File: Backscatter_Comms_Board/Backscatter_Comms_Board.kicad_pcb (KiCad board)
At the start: 2 copper layers, 38.5 x 33.9 mm, 48 parts, among them J1 SPK_IN, J2 Conn_01x09, J3 Conn_01x02, M1 MNMOS, M2 DNP, T1 SP-48, U1 ADG919BRMZ, U2 ADG841YKSZ-REEL7, U3 NCS2200SQ2T2G

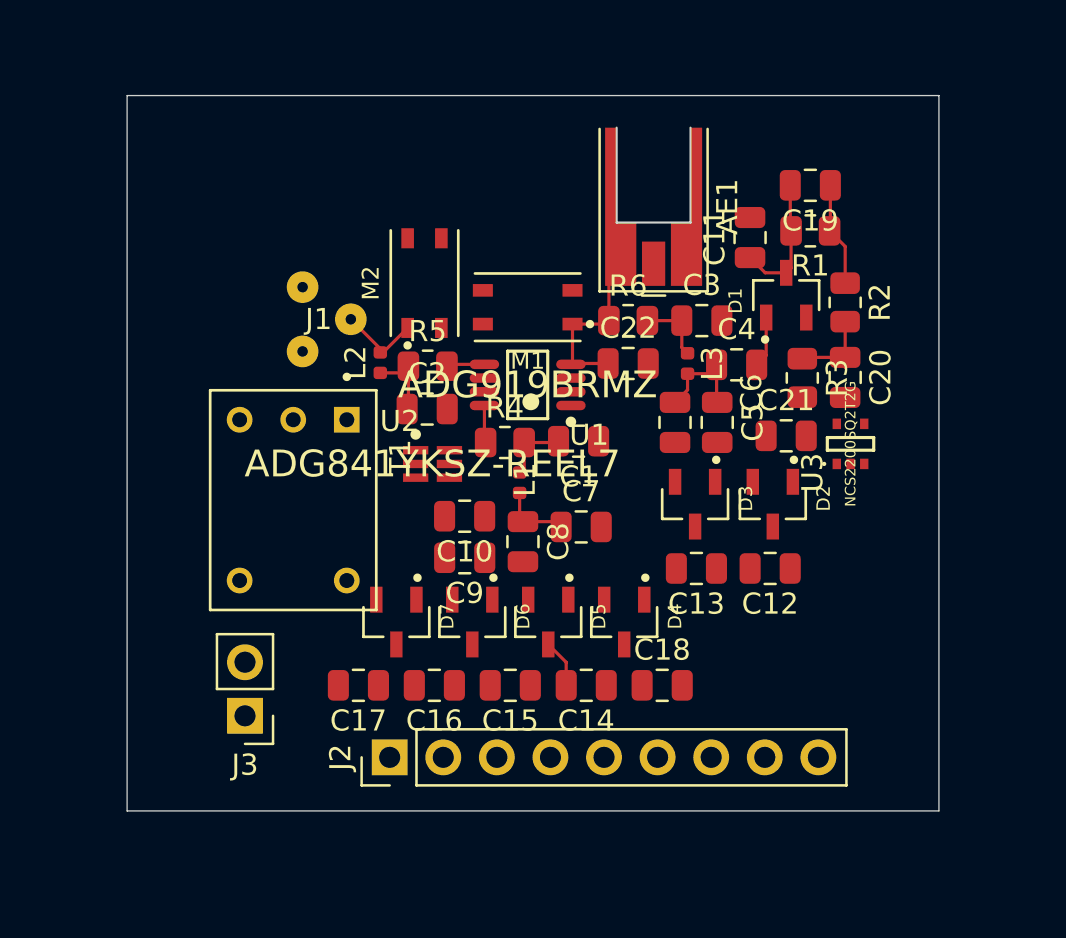
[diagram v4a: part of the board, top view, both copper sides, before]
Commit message: Routed Main components
All components routed except the i/o pins
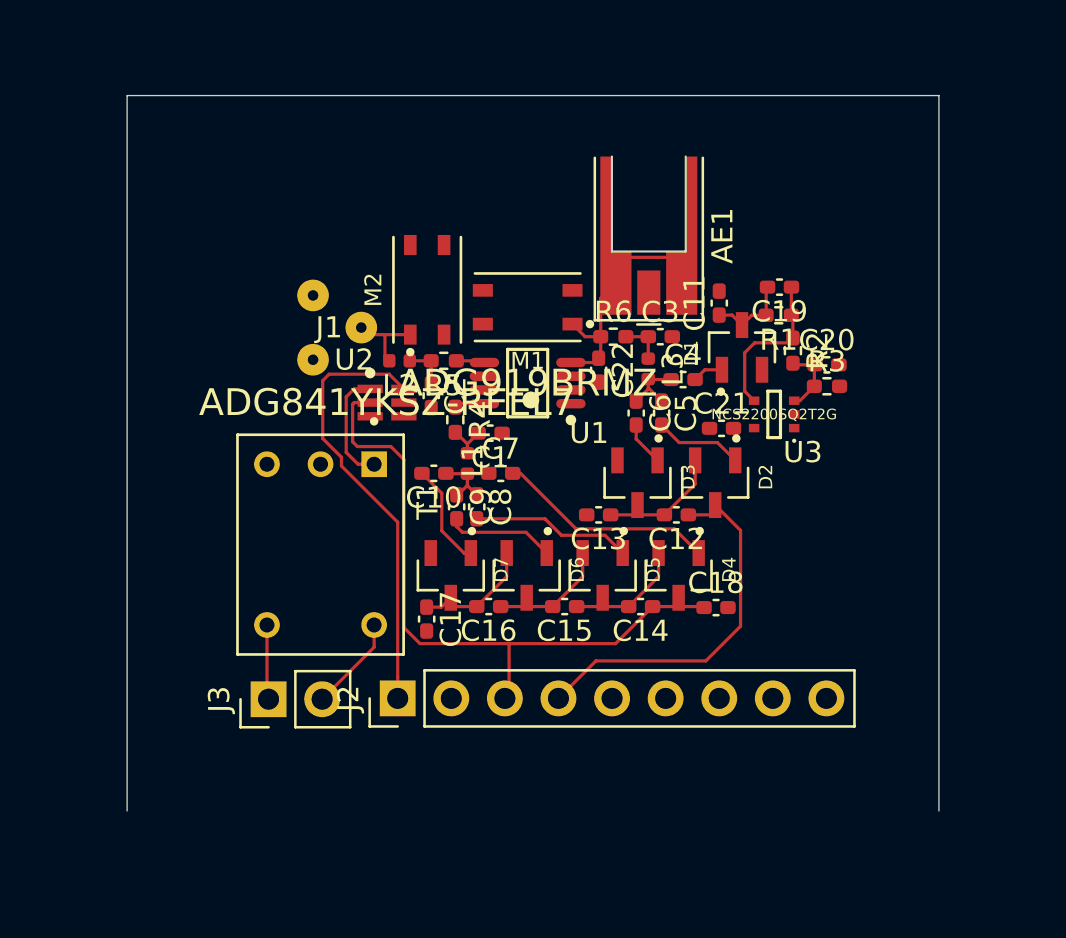
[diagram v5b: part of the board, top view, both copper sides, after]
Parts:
- C1, C10, C11, C12, C13, C14, C15, C16, C17, C18, C19, C2, C20, C21, C22, C3, C4, C5, C6, C7, C8, C9: footprint Capacitor_SMD:C_0805_2012Metric -> Capacitor_SMD:C_0402_1005Metric_Pad0.74x0.62mm_HandSolder
- R1, R2, R3, R4, R5, R6: footprint Resistor_SMD:R_0805_2012Metric -> Resistor_SMD:R_0402_1005Metric_Pad0.72x0.64mm_HandSolder
- moved C13 5.28 mm to (92.8, 25.7)
- moved C12 5.12 mm to (96.5, 25.7)
- moved C19 5.04 mm to (101.4, 14.9)
- moved C7 4.58 mm to (88.2, 23.7)
- moved C15 4.54 mm to (91.2, 30.1)
- moved C14 4.54 mm to (94.8, 30.1)
- moved C16 4.54 mm to (87.6, 30.1)
- moved C17 4.51 mm to (84.7, 30.7), turned to 270 degrees
- moved C18 4.48 mm to (98.4, 30.1)
- moved R1 4.27 mm to (101.4, 16.3)
- moved C1 4.21 mm to (87.7, 21.8)
- moved U3 3.88 mm to (101.2, 21.0), turned to 180 degrees
- moved U2 3.62 mm to (82.8, 20.4)
- moved C11 3.43 mm to (98.6, 15.7)
- moved D5 3.40 mm to (93.0, 28.6)
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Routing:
- net Stage4: track 0.00 -> 31.8 mm
- net Vstore: track 0.00 -> 20.8 mm
- net Vrect: track 0.00 -> 18.0 mm
- net Net-(C7-Pad2): track 0.00 -> 10.4 mm
- net Net-(C8-Pad2): track 0.00 -> 7.59 mm
- net Net-(C12-Pad2): track 0.00 -> 6.20 mm
- net Net-(C16-Pad2): track 0.00 -> 6.09 mm
- net Net-(C15-Pad2): track 0.00 -> 6.01 mm
- net Net-(T1-Pad1): track 0.00 -> 5.48 mm
- net Net-(C9-Pad2): track 0.00 -> 5.16 mm
- net Net-(C10-Pad2): track 0.00 -> 4.93 mm
- net Net-(J3-Pad2): track 0.00 -> 4.54 mm
- net Net-(C5-Pad2): track 0.00 -> 4.18 mm
- net Net-(C14-Pad2): track 2.29 -> 6.03 mm
- net Net-(J3-Pad1): track 0.00 -> 3.55 mm
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
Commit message: Final?
This will be the final of today unless we decide to do a design review
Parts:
- added DNP1: R_DLS, Resistor_SMD:R_0402_1005Metric_Pad0.72x0.64mm_HandSolder, F.Cu at (110.5, 46.4)
- AE1: footprint Connector_Coaxial:MMCX_Molex_73415-0961_Horizontal_1.0mm-PCB -> Connector_Coaxial:MMCX_Molex_73415-0961_Horizontal_0.8mm-PCB
- M1: value MNMOS -> BF1101WR
- M2: value DNP -> BF1101WR
- moved M1 35.2 mm to (117.2, 37.5), turned to 90 degrees
- moved M2 33.4 mm to (109.7, 37.2), turned to 0 degrees
- moved C2 33.4 mm to (111.5, 40.3), turned to 0 degrees
- moved C19 33.3 mm to (127.4, 35.8)
- moved C3 33.3 mm to (121.8, 38.1)
- moved L3 33.3 mm to (121.2, 39.6)
- moved R6 33.3 mm to (119.6, 38.1)
- moved C12 33.3 mm to (122.6, 46.5)
- moved C16 33.3 mm to (113.7, 50.9)
- moved C18 33.3 mm to (124.4, 50.9)
- moved C20 33.3 mm to (129.7, 39.4)
- moved C8 33.3 mm to (113.1, 46.2)
- moved C9 33.3 mm to (112.1, 46.2)
- moved D2 33.3 mm to (124.4, 45.0)
- moved D3 33.3 mm to (120.7, 45.0)
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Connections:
- J2 pad 1: Vstore -> Stage4
- J2 pad 2: RX_EN -> Vstore
- J2 pad 3: Stage4 -> UPLINK_SR
- J2 pad 4: Vrect -> SPK_EN
- J2 pad 5: RF_RX -> RF_TX
- J2 pad 6: RF_TX -> AN_EN
- J2 pad 7: UPLINK_SR -> Vrect
- J2 pad 8: SPK_EN -> RX_EN
- J2 pad 9: AN_EN -> RF_RX
- M1 pad 1: Ant -> GND
- M1 pad 2: RF_TX -> Ant
- M1 pad 3: GND -> RF_TX
- M1 pad 4: GND -> RF_TX
- M2 pad 1: Net-(J1-Pad3) -> GND
- M2 pad 2: UPLINK_SR -> Net-(J1-Pad3)
- M2 pad 3: GND -> UPLINK_SR
- M2 pad 4: GND -> UPLINK_SR
- T1 pad 3: GND -> Net-(DNP1-Pad2)
- U2 pad 3: GND -> Net-(DNP1-Pad2)
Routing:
- net GND: track 0.00 -> 40.2 mm, vias 0 -> 3
- net SPK_EN: track 0.00 -> 23.9 mm, vias 0 -> 1
- net UPLINK_SR: track 0.00 -> 23.2 mm, vias 0 -> 1
- net RF_TX: track 0.00 -> 21.5 mm, vias 0 -> 1
- net AN_EN: track 0.00 -> 16.3 mm, vias 0 -> 1
- net Net-(DNP1-Pad2): track 0.00 -> 15.7 mm, vias 0 -> 1
- net RX_EN: track 0.00 -> 14.2 mm
- net RF_RX: track 0.00 -> 13.4 mm
- net Vrect: track 18.0 -> 12.2 mm
- net Vstore: track 20.8 -> 16.0 mm, vias 0 -> 1
- net Stage4: track 31.8 -> 33.6 mm, vias 0 -> 2
- net Net-(T1-Pad1): track 5.48 -> 7.19 mm
- net Ant: track 12.2 -> 11.2 mm
- net Net-(J1-Pad3): track 3.79 -> 2.99 mm
- net Net-(C7-Pad2): track 10.4 -> 11.1 mm
- added copper zone on B.Cu, net GND
- removed copper zone on B.Cu, net (none)
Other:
- board size 38.5 x 33.9 mm -> 32.5 x 34.6 mm

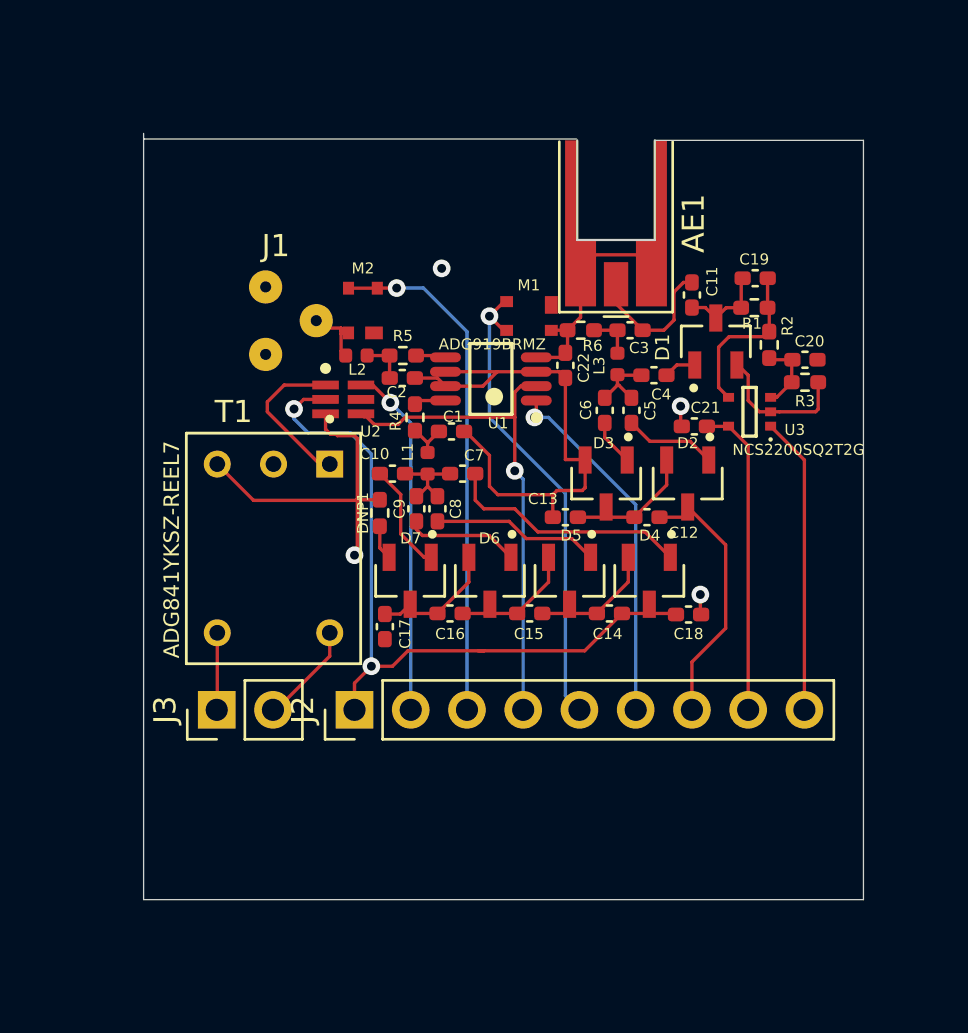
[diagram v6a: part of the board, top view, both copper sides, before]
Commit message: Small fixes final
fixed nmos enclosure(again) and added better text
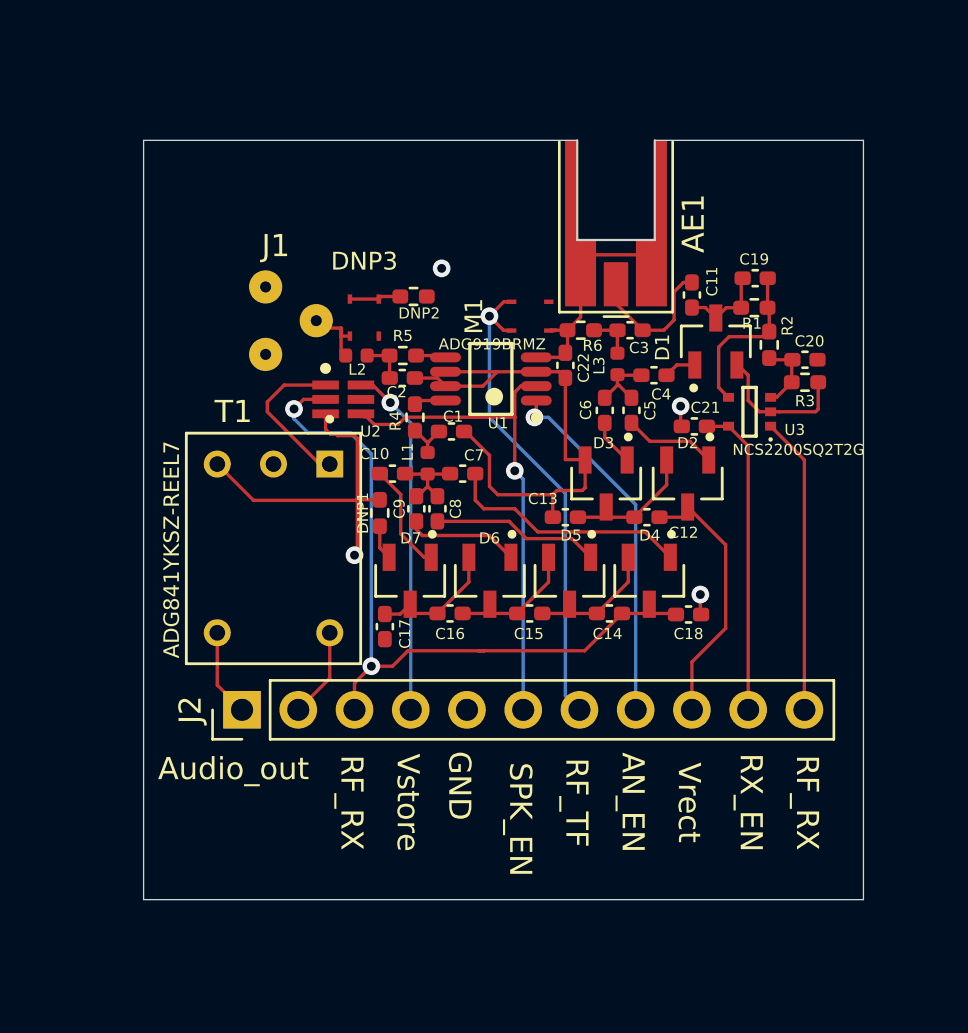
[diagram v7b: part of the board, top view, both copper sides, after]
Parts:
- removed J3: Conn_01x02, Connector_PinHeader_2.54mm:PinHeader_1x02_P2.54mm_Vertical
- removed M2: BF1101WR, Local Components:BF1101WR
- added DNP2: R_DLS, Resistor_SMD:R_0402_1005Metric_Pad0.72x0.64mm_HandSolder, F.Cu at (112.0, 36.6)
- added DNP3: 3SK293, Local Components:3SK293, F.Cu at (109.8, 37.5)
- J2: value Conn_01x09 -> Conn_01x11; footprint Connector_PinHeader_2.54mm:PinHeader_1x09_P2.54mm_Vertical -> Connector_PinHeader_2.54mm:PinHeader_1x11_P2.54mm_Vertical
- M1: value BF1101WR -> 3SK293; footprint Local Components:BF1101WR -> Local Components:3SK293
- moved J2 5.08 mm to (104.3, 55.2)
- moved M1 0.06 mm to (117.3, 37.5)
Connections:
- J2 pad 1: Stage4 -> Net-(J2-Pad1)
- J2 pad 2: Vstore -> Net-(J2-Pad2)
- J2 pad 3: UPLINK_SR -> Stage4
- J2 pad 4: SPK_EN -> Vstore
- J2 pad 5: RF_TX -> GND
- J2 pad 6: AN_EN -> SPK_EN
- J2 pad 7: Vrect -> RF_TX
- J2 pad 8: RX_EN -> AN_EN
- J2 pad 9: RF_RX -> Vrect
- M1 pad 1: GND -> Ant
- M1 pad 2: Ant -> GND
- T1 pad 4: Net-(J3-Pad1) -> Net-(J2-Pad1)
- T1 pad 5: Net-(J3-Pad2) -> Net-(J2-Pad2)
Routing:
- net UPLINK_SR: track 23.2 -> 0.00 mm, vias 1 -> 0
- net Net-(J3-Pad2): track 4.54 -> 0.00 mm
- net Net-(J2-Pad2): track 0.00 -> 4.07 mm
- net Net-(J2-Pad1): track 0.00 -> 3.94 mm
- net Net-(J3-Pad1): track 3.55 -> 0.00 mm
- net Net-(DNP2-Pad2): track 0.00 -> 2.32 mm
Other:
- board size 32.5 x 34.6 mm -> 32.5 x 34.3 mm
- board text added: "AN_EN"
- board text added: "Audio_out"
- board text added: "GND"
- board text added: "RF_RX"
- board text added: "RF_TF"
- board text added: "RX_EN"
- board text added: "SPK_EN"
- board text added: "Vrect"
- board text added: "Vstore"
